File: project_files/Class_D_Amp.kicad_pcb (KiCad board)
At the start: 2 copper layers, 100 x 100 mm, 81 parts, among them P1 ROUT, P2 LOUT, P3 CONN_01X04, P4 2x12V, Q1 BC847, Q2 BC857, Q3 IPD180N10, Q4 IPD180N10, Q5 IPD180N10, Q6 IPD180N10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

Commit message: Clustered modules together
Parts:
- added C34: 10n, Capacitors_SMD:C_0805, F.Cu at (143.0, 37.0)
- added C35: 10n, Capacitors_SMD:C_0805, F.Cu at (201.0, 42.0)
- moved C23 92.6 mm to (57.0, 90.5)
- moved R11 92.2 mm to (58.5, 85.0), turned to 270 degrees
- moved R12 90.7 mm to (60.5, 83.0), turned to 270 degrees
- moved R23 86.4 mm to (62.5, 97.0), turned to 270 degrees
- moved C32 81.7 mm to (226.0, 79.0)
- moved R24 81.4 mm to (67.5, 97.0), turned to 270 degrees
- moved R17 80.8 mm to (70.5, 84.0), turned to 270 degrees
- moved C16 78.5 mm to (227.0, 104.0), turned to 180 degrees
- moved R13 78.3 mm to (72.5, 86.0), turned to 270 degrees
- moved C28 76.9 mm to (73.0, 90.5)
- moved C17 74.8 mm to (223.0, 112.0)
- moved C1 74.3 mm to (177.0, 92.0)
- moved R21 73.2 mm to (218.0, 82.0), turned to 270 degrees
- moved R14 71.8 mm to (220.0, 112.0), turned to 270 degrees
- moved C30 71.6 mm to (220.0, 108.0), turned to 90 degrees
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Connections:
- C1 pad 1: +12V -> /VSS+12V
- C1 pad 2: GND -> VSS
- C15 pad 1: +12V -> /VSS+12V
- C15 pad 2: GND -> VSS
- C19 pad 2: Net-(C19-Pad1) -> Net-(C19-Pad2)
- C7 pad 2: Net-(C7-Pad1) -> Net-(C7-Pad2)
- D1 pad 1: Net-(D1-Pad1) -> GND
- D1 pad 2: GND -> (no net)
- D1 pad 3: (no net) -> Net-(D1-Pad3)
- D2 pad 1: GND -> Net-(D2-Pad1)
- D2 pad 2: Net-(D2-Pad2) -> (no net)
- D2 pad 3: (no net) -> GND
- L1 pad 1: Net-(C7-Pad1) -> Net-(C7-Pad2)
- L2 pad 1: Net-(C19-Pad1) -> Net-(C19-Pad2)
- Q1 pad 1: Net-(D1-Pad1) -> Net-(D1-Pad3)
- Q2 pad 1: Net-(D2-Pad2) -> Net-(D2-Pad1)
- Q3 pad 3: Net-(C7-Pad1) -> Net-(C7-Pad2)
- Q4 pad 2: Net-(C7-Pad1) -> Net-(C7-Pad2)
- Q5 pad 3: Net-(C19-Pad1) -> Net-(C19-Pad2)
- Q6 pad 2: Net-(C19-Pad1) -> Net-(C19-Pad2)
- R1 pad 1: Net-(D1-Pad1) -> Net-(D1-Pad3)
- R10 pad 1: Net-(C7-Pad1) -> Net-(C7-Pad2)
- R15 pad 1: Net-(C19-Pad1) -> Net-(C19-Pad2)
- R2 pad 1: Net-(D2-Pad2) -> Net-(D2-Pad1)
- R22 pad 1: Net-(C19-Pad1) -> Net-(C19-Pad2)
- R4 pad 1: Net-(C7-Pad1) -> Net-(C7-Pad2)
- U2 pad 4: Net-(C7-Pad1) -> Net-(C7-Pad2)
- U6 pad 4: Net-(C19-Pad1) -> Net-(C19-Pad2)

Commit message: Updated PCB design
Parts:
- moved C16 183.0 mm to (44.0, 105.5), turned to 0 degrees
- moved U5 179.1 mm to (46.0, 101.7), turned to 180 degrees
- moved C18 177.5 mm to (36.7, 103.6), turned to 270 degrees
- moved C21 177.3 mm to (36.7, 99.7), turned to 90 degrees
- moved L2 175.6 mm to (40.0, 39.0)
- moved C17 175.5 mm to (48.0, 97.8), turned to 180 degrees
- moved C32 175.5 mm to (50.5, 77.5), turned to 270 degrees
- moved P2 174.6 mm to (43.0, 19.0)
- moved Q6 174.3 mm to (45.7, 72.9)
- moved R21 174.3 mm to (43.7, 80.9)
- moved C20 174.3 mm to (31.0, 30.0)
- moved Q5 173.4 mm to (37.6, 72.9)
- moved R16 173.4 mm to (35.6, 80.9)
- moved C31 173.3 mm to (32.8, 76.8), turned to 270 degrees
- moved D5 171.9 mm to (39.4, 104.7), turned to 180 degrees
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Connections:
- net Net-(C19-Pad2) renamed /LNODE
- net Net-(C20-Pad1) renamed /LOUT
- net Net-(C34-Pad1) renamed /ROUT
- net Net-(C7-Pad2) renamed /RNODE
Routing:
- net /LNODE: track 0.00 -> 67.5 mm, vias 0 -> 2
- net GND: track 0.00 -> 39.8 mm, vias 0 -> 26
- net Net-(R17-Pad1): track 0.00 -> 25.5 mm, vias 0 -> 2
- net /RNODE: track 0.00 -> 24.6 mm
- net Net-(R12-Pad1): track 0.00 -> 21.9 mm
- net /LOUT: track 0.00 -> 20.7 mm
- net Net-(C18-Pad1): track 0.00 -> 18.6 mm
- net Net-(R21-Pad2): track 0.00 -> 16.9 mm
- net /ROUT: track 0.00 -> 16.3 mm
- net Net-(R16-Pad2): track 0.00 -> 14.0 mm
- net VSS: track 0.00 -> 13.3 mm
- net +12V: track 0.00 -> 11.8 mm
- net -12V: track 0.00 -> 11.6 mm
- net Net-(C21-Pad1): track 0.00 -> 11.5 mm
- net Net-(R23-Pad2): track 0.00 -> 11.0 mm
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- added copper zone on F.Cu, net /LNODE
- added copper zone on F.Cu, net /RNODE
- added copper zone on F.Cu, net VDD
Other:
- net class Default: clearance 0.2 -> 0.25; trace_width 0.25 -> 0.3
- net class Power added: clearance 0.3, trace_width 0.5, via_dia 1, via_drill 0.6
- net class Switching added: clearance 0.3, trace_width 0.5, via_dia 1, via_drill 0.6
- rule trace_clearance: 0.2 -> 0.25

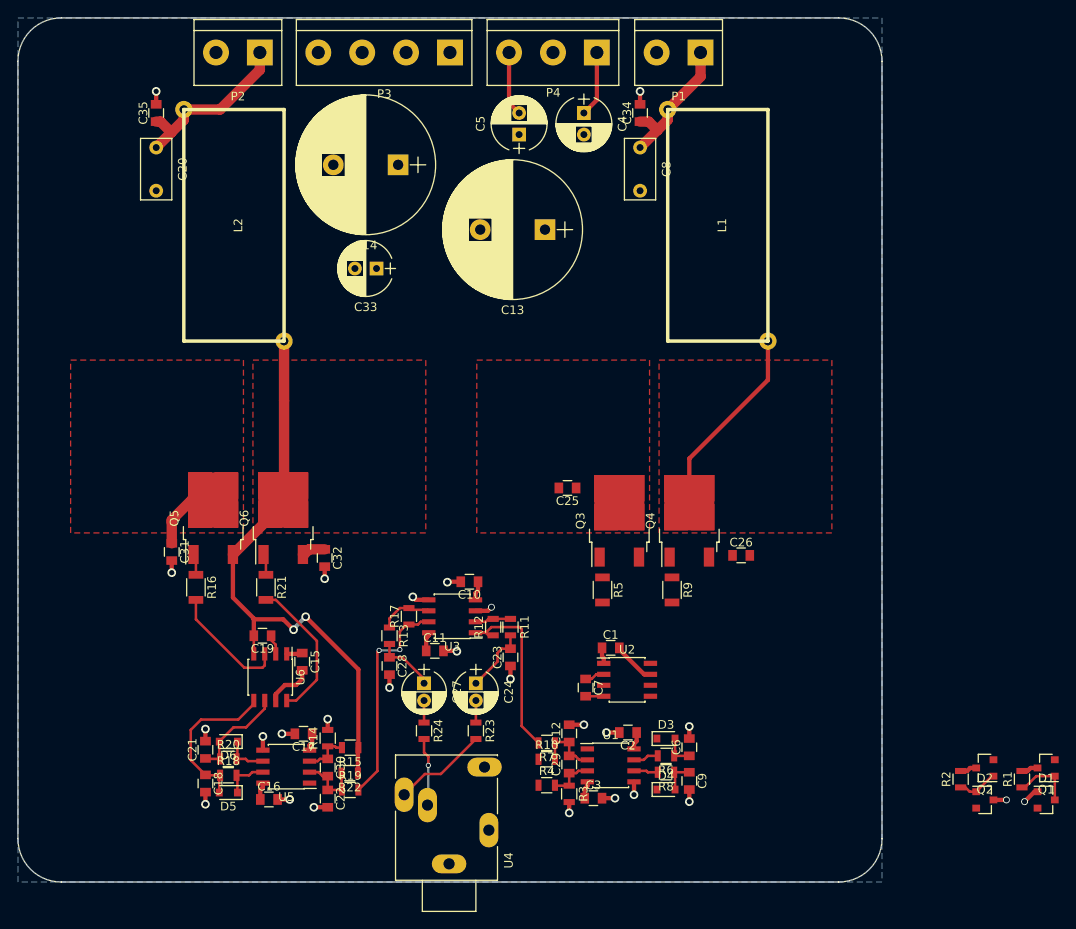
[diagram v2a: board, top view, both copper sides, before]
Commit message: Fixed Thermal pads
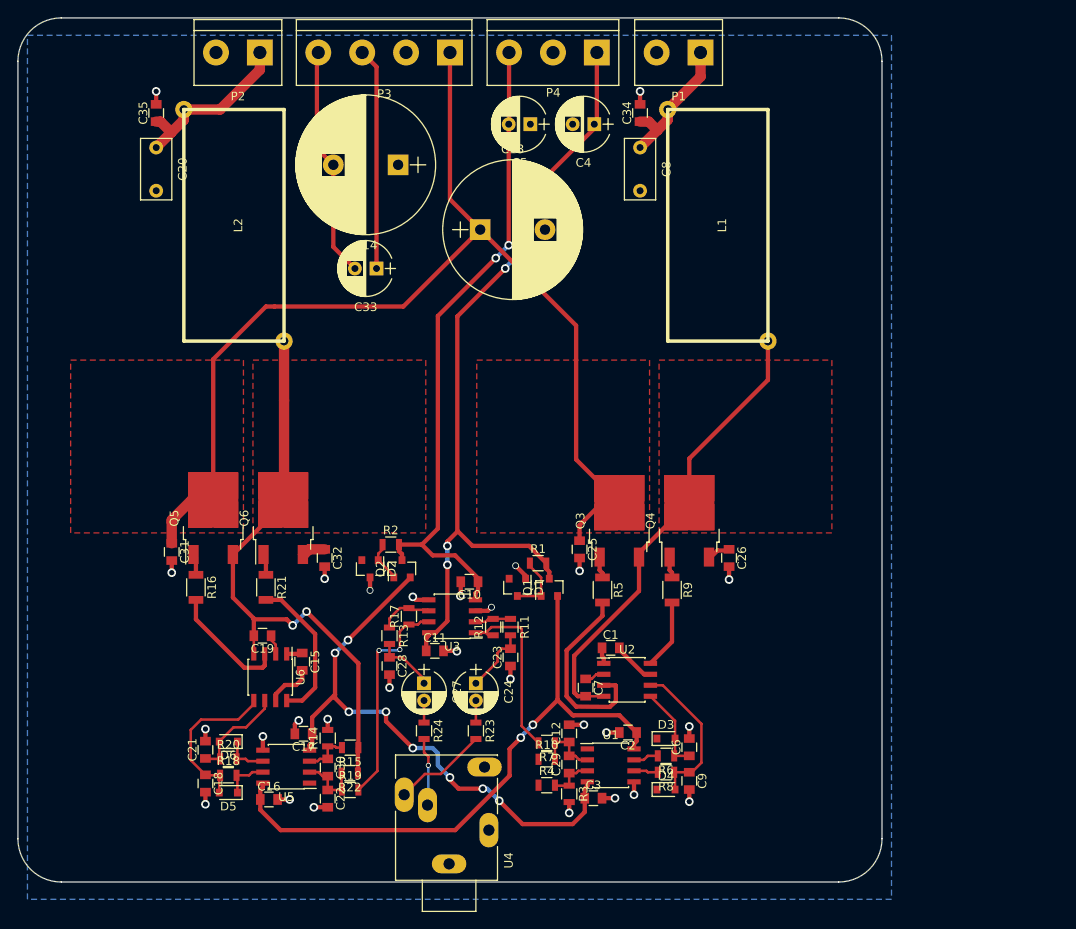
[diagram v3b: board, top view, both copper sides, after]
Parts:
- moved D2 76.0 mm to (55.8, 78.8), turned to 270 degrees
- moved R2 71.3 mm to (58.1, 76.0), turned to 0 degrees
- moved Q2 71.3 mm to (59.5, 78.8), turned to 90 degrees
- moved D1 66.0 mm to (72.8, 80.9), turned to 270 degrees
- moved R1 61.3 mm to (75.2, 78.1), turned to 0 degrees
- moved Q1 61.2 mm to (76.5, 80.9), turned to 90 degrees
- moved C13 7.50 mm to (68.5, 39.5), turned to 0 degrees
- moved C25 7.24 mm to (80.0, 76.5), turned to 270 degrees
- moved C4 1.77 mm to (81.7, 27.3), turned to 180 degrees
- moved C5 1.77 mm to (74.3, 27.3), turned to 180 degrees
- moved C26 1.43 mm to (97.3, 77.5), turned to 270 degrees
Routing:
- net VDD: track 8.45 -> 129.6 mm
- net +12V: track 11.8 -> 91.8 mm, vias 0 -> 4
- net +5V: track 4.04 -> 71.5 mm, vias 0 -> 2
- net -12V: track 11.6 -> 76.5 mm, vias 0 -> 2
- net -5V: track 4.04 -> 66.0 mm, vias 0 -> 8
- net VSS: track 13.3 -> 42.9 mm
- net /RNODE: track 24.6 -> 53.6 mm
- net /VSS+12V: track 3.71 -> 29.4 mm
- net Net-(R5-Pad2): track 0.00 -> 22.3 mm
- net Net-(C9-Pad1): track 3.79 -> 17.9 mm
- net Net-(R9-Pad2): track 0.00 -> 8.08 mm
- net Net-(C6-Pad1): track 3.79 -> 9.87 mm
- net GND: track 39.8 -> 43.2 mm, vias 26 -> 28
- net Net-(Q3-Pad1): track 0.00 -> 2.49 mm
- net Net-(Q4-Pad1): track 0.00 -> 2.47 mm
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
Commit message: Completed first revision of board
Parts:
- added REF**: MountingHole_3.2mm_M3, Mounting_Holes:MountingHole_3.2mm_M3, F.Cu at (24.0, 19.0)
- added REF**: MountingHole_3.2mm_M3, Mounting_Holes:MountingHole_3.2mm_M3, F.Cu at (24.0, 111.0)
- added REF**: MountingHole_3.2mm_M3, Mounting_Holes:MountingHole_3.2mm_M3, F.Cu at (106.0, 19.0)
- added REF**: MountingHole_3.2mm_M3, Mounting_Holes:MountingHole_3.2mm_M3, F.Cu at (106.0, 111.0)
- moved D2 1.06 mm to (55.0, 79.5)
- moved Q2 1.06 mm to (58.7, 79.5)
- moved R2 1.06 mm to (57.4, 76.7)
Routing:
- net VSS: track 42.9 -> 193.7 mm, vias 0 -> 2
- net /VSS+12V: track 29.4 -> 125.0 mm, vias 0 -> 8
- net GND: track 43.2 -> 66.9 mm, vias 28 -> 40
- net /RNODE: track 53.6 -> 68.8 mm, vias 0 -> 2
- net Net-(R5-Pad2): track 22.3 -> 14.3 mm, vias 0 -> 4
- net VDD: track 129.6 -> 132.4 mm
- net -12V: track 76.5 -> 79.2 mm
- net Net-(D4-Pad1): track 2.82 -> 4.86 mm
- net Net-(D3-Pad1): track 2.94 -> 4.98 mm
- net /LNODE: track 67.9 -> 69.8 mm, vias 2 -> 4
- net Net-(R21-Pad2): track 17.5 -> 18.9 mm, vias 0 -> 2
- net +12V: track 91.8 -> 93.0 mm
- net +5V: track 71.5 -> 72.6 mm, vias 2 -> 6
- net -5V: track 66.0 -> 64.9 mm
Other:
- board size 100 x 100 mm -> 90 x 100 mm
- board text added: "2ch 50W Class D Amplifier By Jacob Bechmann Pedersen & Mikkel Bjerg Petersen 2018-01-08 E5SPK @ Aarhus Universitet Herning"

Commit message: Generated Gerbers
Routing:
- net GND: track 66.9 -> 43.2 mm, vias 40 -> 28
- net (no net): track 0.00 -> 23.7 mm, vias 0 -> 12
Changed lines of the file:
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@@
     (links 176)
     (no_connects 0)
-    (area 19.924999 14.924999 110.075001 115.075001)
+    (area 14.342857 12.845 116.100001 119.125001)
     (thickness 1.6)
     (drawings 9)
@@
     (visible_elements FFFEFF7F)
     (pcbplotparams
-      (layerselection 0x00030_80000001)
+      (layerselection 0x010f0_80000001)
       (usegerberextensions false)
-      (excludeedgelayer true)
-      (linewidth 0.100000)
-      (plotframeref true)
+      (usegerberattributes true)
+      (excludeedgelayer false)
+      (linewidth 0.150000)
+      (plotframeref false)
       (viasonmask false)
       (mode 1)
-      (useauxorigin false)
+      (useauxorigin true)
       (hpglpennumber 1)
       (hpglpenspeed 20)
@@
       (padsonsilk false)
       (subtractmaskfromsilk false)
-      (outputformat 4)
+      (outputformat 1)
       (mirror false)
       (drillshape 0)
       (scaleselection 1)
-      (outputdirectory ""))
+      (outputdirectory plots/))
   )
   (net 0 "")
@@
   (gr_arc (start 105 20) (end 105 15) (angle 90) (layer Edge.Cuts) (width 0.15))
   (gr_arc (start 105 110) (end 110 110) (angle 90) (layer Edge.Cuts) (width 0.15))
+  (via (at 70.9 53.9) (size 0.6) (drill 0.4) (layers F.Cu B.Cu) (net 0))
+  (via (at 73.45 51.4) (size 0.6) (drill 0.4) (layers F.Cu B.Cu) (net 0))
+  (segment (start 73.45 51.4) (end 70.95 53.9) (width 0.3) (layer F.Cu) (net 0))
+  (segment (start 70.95 53.9) (end 70.9 53.9) (width 0.3) (layer F.Cu) (net 0))
+  (via (at 88.65 70) (size 0.6) (drill 0.4) (layers F.Cu B.Cu) (net 0))
+  (via (at 88.65 66.5) (size 0.6) (drill 0.4) (layers F.Cu B.Cu) (net 0))
+  (segment (start 88.65 70) (end 88.65 66.5) (width 0.3) (layer F.Cu) (net 0))
+  (via (at 53.5 46.75) (size 1) (drill 0.6) (layers F.Cu B.Cu) (net 0))
+  (via (at 49.25 46.75) (size 1) (drill 0.6) (layers F.Cu B.Cu) (net 0))
+  (segment (start 53.5 46.75) (end 49.25 46.75) (width 1.22) (layer F.Cu) (net 0))
+  (segment (start 53.75 53.5) (end 53.5 53.5) (width 1.22) (layer B.Cu) (net 0))
+  (via (at 49.5 53.5) (size 1) (drill 0.6) (layers F.Cu B.Cu) (net 0))
+  (segment (start 53.5 53.5) (end 49.5 53.5) (width 1.22) (layer F.Cu) (net 0))
+  (via (at 53.5 53.5) (size 1) (drill 0.6) (layers F.Cu B.Cu) (net 0))
+  (via (at 63.75 47) (size 1) (drill 0.6) (layers F.Cu B.Cu) (net 0))
+  (via (at 66.5 44.25) (size 1) (drill 0.6) (layers F.Cu B.Cu) (net 0))
+  (segment (start 63.75 47) (end 66.5 44.25) (width 1.22) (layer F.Cu) (net 0))
+  (via (at 67 50.75) (size 1) (drill 0.6) (layers F.Cu B.Cu) (net 0))
+  (via (at 70 47.75) (size 1) (drill 0.6) (layers F.Cu B.Cu) (net 0))
+  (segment (start 67 50.75) (end 70 47.75) (width 1.22) (layer F.Cu) (net 0))
   (segment (start 76.15 78.1) (end 76.15 77.9) (width 0.5) (layer F.Cu) (net 1))
   (segment (start 76.15 77.9) (end 75 76.75) (width 0.5) (layer F.Cu) (net 1))
@@
   (segment (start 62.55 86.45) (end 62.25 86.75) (width 0.5) (layer F.Cu) (net 1))
   (segment (start 62.25 86.75) (end 62.25 88.25) (width 0.5) (layer F.Cu) (net 1))
-  (via (at 70.9 53.9) (size 0.6) (drill 0.4) (layers F.Cu B.Cu) (net 2))
-  (via (at 73.45 51.4) (size 0.6) (drill 0.4) (layers F.Cu B.Cu) (net 2))
-  (segment (start 73.45 51.4) (end 70.95 53.9) (width 0.3) (layer F.Cu) (net 2))
-  (segment (start 70.95 53.9) (end 70.9 53.9) (width 0.3) (layer F.Cu) (net 2))
-  (via (at 88.65 70) (size 0.6) (drill 0.4) (layers F.Cu B.Cu) (net 2))
-  (via (at 88.65 66.5) (size 0.6) (drill 0.4) (layers F.Cu B.Cu) (net 2))
-  (segment (start 88.65 70) (end 88.65 66.5) (width 0.3) (layer F.Cu) (net 2))
-  (via (at 53.5 46.75) (size 1) (drill 0.6) (layers F.Cu B.Cu) (net 2))
-  (via (at 49.25 46.75) (size 1) (drill 0.6) (layers F.Cu B.Cu) (net 2))
-  (segment (start 53.5 46.75) (end 49.25 46.75) (width 1.22) (layer F.Cu) (net 2))
-  (segment (start 53.75 53.5) (end 53.5 53.5) (width 1.22) (layer B.Cu) (net 2))
-  (via (at 49.5 53.5) (size 1) (drill 0.6) (layers F.Cu B.Cu) (net 2))
-  (segment (start 53.5 53.5) (end 49.5 53.5) (width 1.22) (layer F.Cu) (net 2))
-  (via (at 53.5 53.5) (size 1) (drill 0.6) (layers F.Cu B.Cu) (net 2))
-  (via (at 63.75 47) (size 1) (drill 0.6) (layers F.Cu B.Cu) (net 2))
-  (via (at 66.5 44.25) (size 1) (drill 0.6) (layers F.Cu B.Cu) (net 2))
-  (segment (start 63.75 47) (end 66.5 44.25) (width 1.22) (layer F.Cu) (net 2))
-  (via (at 67 50.75) (size 1) (drill 0.6) (layers F.Cu B.Cu) (net 2))
-  (via (at 70 47.75) (size 1) (drill 0.6) (layers F.Cu B.Cu) (net 2))
-  (segment (start 67 50.75) (end 70 47.75) (width 1.22) (layer F.Cu) (net 2))
   (segment (start 55 80.5) (end 55 82) (width 0.5) (layer F.Cu) (net 2))
   (via (at 55 82) (size 1) (drill 0.6) (layers F.Cu B.Cu) (net 2))

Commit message: fixed size
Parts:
- moved REF** 1.00 mm to (106.0, 20.0)
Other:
- board size 90 x 100 mm -> 90 x 99 mm
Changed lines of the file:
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@@
   )
   (module Mounting_Holes:MountingHole_3.2mm_M3 (layer F.Cu)
-    (at 106 19)
+    (at 106 20)
     (descr "Mounting Hole 3.2mm, no annular, M3")
     (tags "mounting hole 3.2mm no annular m3")
@@
     (pad 1 np_thru_hole circle (at 0 0) (size 3.2 3.2) (drill 3.2) (layers *.Cu *.Mask))
   )
+  (gr_line (start 110 21) (end 110 110) (angle 90) (layer Edge.Cuts) (width 0.15))
+  (gr_line (start 20 21) (end 20 110) (angle 90) (layer Edge.Cuts) (width 0.15))
   (gr_text "2ch 50W Class D Amplifier\nBy Jacob Bechmann Pedersen\n& Mikkel Bjerg Petersen\n2018-01-08\nE5SPK @ Aarhus Universitet Herning" (at 65 61) (layer F.SilkS)
     (effects (font (size 1.5 1.5) (thickness 0.3)))
   )
-  (gr_line (start 105 15) (end 25 15) (angle 90) (layer Edge.Cuts) (width 0.15))
+  (gr_line (start 105 16) (end 25 16) (angle 90) (layer Edge.Cuts) (width 0.15))
   (gr_line (start 25 115) (end 105 115) (angle 90) (layer Edge.Cuts) (width 0.15))
-  (gr_line (start 110 110) (end 110 20) (angle 90) (layer Edge.Cuts) (width 0.15))
-  (gr_line (start 20 110) (end 20 20) (angle 90) (layer Edge.Cuts) (width 0.15))
   (gr_arc (start 25 110) (end 25 115) (angle 90) (layer Edge.Cuts) (width 0.15))
-  (gr_arc (start 25 20) (end 20 20) (angle 90) (layer Edge.Cuts) (width 0.15))
-  (gr_arc (start 105 20) (end 105 15) (angle 90) (layer Edge.Cuts) (width 0.15))
+  (gr_arc (start 25 21) (end 20 21) (angle 90) (layer Edge.Cuts) (width 0.15))
+  (gr_arc (start 105 21) (end 105 16) (angle 90) (layer Edge.Cuts) (width 0.15))
   (gr_arc (start 105 110) (end 110 110) (angle 90) (layer Edge.Cuts) (width 0.15))
   (via (at 70.9 53.9) (size 0.6) (drill 0.4) (layers F.Cu B.Cu) (net 0))

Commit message: Completed Board Layout
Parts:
- removed D3, D4, D5, D6: TS4148RY, Diodes_SMD:D_0805
- removed the REF** at (24.0, 19.0)
- removed the REF** at (24.0, 111.0)
- removed the REF** at (106.0, 20.0)
- removed the REF** at (106.0, 111.0)
- added C36: 47p, Capacitors_SMD:C_0805, F.Cu at (94.2, 100.2)
- added C37: 47p, Capacitors_SMD:C_0805, F.Cu at (36.5, 103.2)
- added C38: 100n, Capacitors_SMD:C_0805, F.Cu at (88.8, 96.5)
- added C39: 100n, Capacitors_SMD:C_0805, F.Cu at (39.2, 106.0)
- added Q10: BC857, TO_SOT_Packages_SMD:SOT-23, F.Cu at (31.8, 98.8)
- added Q11: BC847, TO_SOT_Packages_SMD:SOT-23, F.Cu at (91.4, 100.4)
- added Q12: BC847, TO_SOT_Packages_SMD:SOT-23, F.Cu at (39.4, 102.4)
- added Q13: BC857, TO_SOT_Packages_SMD:SOT-23, F.Cu at (91.4, 96.6)
- added Q14: BC857, TO_SOT_Packages_SMD:SOT-23, F.Cu at (39.4, 98.6)
- added Q7: BC847, TO_SOT_Packages_SMD:SOT-23, F.Cu at (98.9, 100.4)
- added Q8: BC847, TO_SOT_Packages_SMD:SOT-23, F.Cu at (31.8, 102.5)
- added Q9: BC857, TO_SOT_Packages_SMD:SOT-23, F.Cu at (98.9, 96.6)
- added R25: 1k, Resistors_SMD:R_0805, F.Cu at (27.0, 101.0)
- added R26: 2.2k, Resistors_SMD:R_0805, F.Cu at (31.0, 95.2)
- added R27: 2.2k, Resistors_SMD:R_0805, F.Cu at (94.2, 103.8)
- added R28: 2.2k, Resistors_SMD:R_0805, F.Cu at (36.5, 99.8)
- added R29: 1k, Resistors_SMD:R_0805, F.Cu at (94.2, 96.8)
- added R30: 2.2k, Resistors_SMD:R_0805, F.Cu at (91.2, 93.8)
- added R31: 1k, Resistors_SMD:R_0805, F.Cu at (34.5, 101.0)
- added R32: 2.2k, Resistors_SMD:R_0805, F.Cu at (38.2, 95.2)
- added REF**: MountingHole_3.2mm_M3, Mounting_Holes:MountingHole_3.2mm_M3, F.Cu at (105.0, 21.0)
- added REF**: MountingHole_3.2mm_M3, Mounting_Holes:MountingHole_3.2mm_M3, F.Cu at (105.0, 110.0)
- added REF**: MountingHole_3.2mm_M3, Mounting_Holes:MountingHole_3.2mm_M3, F.Cu at (25.0, 110.0)
- added REF**: MountingHole_3.2mm_M3, Mounting_Holes:MountingHole_3.2mm_M3, F.Cu at (25.0, 21.0)
- C18, C21: value 120p -> 100n
- C6, C9: value 120p -> 47p
- R20, R6, R8: value 1k -> 2.2k
- moved C9 63.7 mm to (29.0, 103.2), turned to 90 degrees
- moved R18 62.6 mm to (101.6, 96.6), turned to 270 degrees
- moved R8 61.1 mm to (29.0, 99.8), turned to 270 degrees
- moved C18 60.0 mm to (96.2, 96.5), turned to 90 degrees
- moved R20 59.8 mm to (98.8, 93.8), turned to 180 degrees
- moved R6 12.5 mm to (102.5, 101.2)
- moved C6 9.93 mm to (102.6, 99.4), turned to 180 degrees
- moved C21 8.21 mm to (31.8, 106.2), turned to 270 degrees
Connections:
- C18 pad 1: Net-(C18-Pad1) -> +5V
- C21 pad 1: Net-(C21-Pad1) -> +5V
- C6 pad 1: Net-(C6-Pad1) -> +5V
- C6 pad 2: GND -> Net-(C6-Pad2)
- C9 pad 1: Net-(C9-Pad1) -> +5V
- C9 pad 2: GND -> Net-(C9-Pad2)
- R18 pad 1: Net-(C18-Pad1) -> Net-(Q9-Pad2)
- R18 pad 2: Net-(D5-Pad1) -> +5V
- R20 pad 1: Net-(C21-Pad1) -> VSS
- R20 pad 2: Net-(D6-Pad1) -> /RLI
- R6 pad 1: Net-(C6-Pad1) -> GND
- R6 pad 2: Net-(D3-Pad1) -> Net-(C6-Pad2)
- R8 pad 1: Net-(C9-Pad1) -> GND
- R8 pad 2: Net-(D4-Pad1) -> Net-(C9-Pad2)
- U1 pad 6: Net-(D4-Pad1) -> /ROUT2
- U1 pad 7: Net-(D3-Pad1) -> /ROUT1
- U2 pad 5: Net-(C6-Pad1) -> /RHI
- U2 pad 6: Net-(C9-Pad1) -> /RLI
- U5 pad 6: Net-(D6-Pad1) -> /LOUT2
- U5 pad 7: Net-(D5-Pad1) -> /LOUT1
- U6 pad 5: Net-(C18-Pad1) -> /LHI
- U6 pad 6: Net-(C21-Pad1) -> /LLI
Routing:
- net +5V: track 72.6 -> 160.5 mm, vias 6 -> 8
- net VSS: track 193.7 -> 234.7 mm, vias 2 -> 6
- net Net-(C18-Pad1): track 18.6 -> 0.00 mm
- net Net-(C9-Pad1): track 17.9 -> 0.00 mm
- net /LLI: track 0.00 -> 17.9 mm, vias 0 -> 2
- net /ROUT1: track 0.00 -> 16.2 mm
- net /LOUT1: track 0.00 -> 14.7 mm, vias 0 -> 2
- net /RLI: track 0.00 -> 13.7 mm, vias 0 -> 2
- net Net-(C21-Pad1): track 11.5 -> 0.00 mm
- net Net-(C36-Pad2): track 0.00 -> 10.3 mm, vias 0 -> 2
- net Net-(C6-Pad1): track 9.87 -> 0.00 mm
- net Net-(C9-Pad2): track 0.00 -> 9.42 mm
- net Net-(C37-Pad2): track 0.00 -> 8.97 mm
- net Net-(C6-Pad2): track 0.00 -> 8.78 mm, vias 0 -> 2
- net /LHI: track 0.00 -> 8.69 mm
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
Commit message: Generated Gerbers
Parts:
- renumbered REF** to ?
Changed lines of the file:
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@@
     (tags "mounting hole 3.2mm no annular m3")
     (attr virtual)
-    (fp_text reference REF** (at 0 -4.2) (layer F.SilkS)
+    (fp_text reference "" (at 0 -4.2) (layer F.SilkS)
       (effects (font (size 1 1) (thickness 0.15)))
     )
@@
     (tags "mounting hole 3.2mm no annular m3")
     (attr virtual)
-    (fp_text reference REF** (at 0 -4.2) (layer F.SilkS)
+    (fp_text reference "" (at 0 -4.2) (layer F.SilkS)
       (effects (font (size 1 1) (thickness 0.15)))
     )
@@
     (tags "mounting hole 3.2mm no annular m3")
     (attr virtual)
-    (fp_text reference REF** (at 0 -4.2) (layer F.SilkS)
+    (fp_text reference "" (at 0 -4.2) (layer F.SilkS)
       (effects (font (size 1 1) (thickness 0.15)))
     )
@@
     (tags "mounting hole 3.2mm no annular m3")
     (attr virtual)
-    (fp_text reference REF** (at 0 -4.2) (layer F.SilkS)
+    (fp_text reference "" (at 0 -4.2) (layer F.SilkS)
       (effects (font (size 1 1) (thickness 0.15)))
     )
